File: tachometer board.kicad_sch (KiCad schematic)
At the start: 5 parts, among them J1 Conn_01x04

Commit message: Add README.md
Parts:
- R1, R2: Part Number (none) -> CRCW1210470RFKEA
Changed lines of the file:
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@@
     (pin "4")
     (instances
-      (project "protean board"
+      (project "tachometer board"
         (path "/e74b6ee1-b9f5-4a36-af13-778b210f46d3"
           (reference "U1") (unit 1)
@@
       (effects (font (size 1.27 1.27)) hide)
     )
-    (pin "1")
-    (pin "2")
-    (instances
-      (project "protean board"
+    (property "Part Number" "CRCW1210470RFKEA" (at 168.275 74.295 0)
+      (effects (font (size 1.27 1.27)) hide)
+    )
+    (pin "1")
+    (pin "2")
+    (instances
+      (project "tachometer board"
         (path "/e74b6ee1-b9f5-4a36-af13-778b210f46d3"
           (reference "R2") (unit 1)
@@
     (pin "1")
     (instances
-      (project "protean board"
+      (project "tachometer board"
         (path "/e74b6ee1-b9f5-4a36-af13-778b210f46d3"
           (reference "#PWR04") (unit 1)
@@
     (pin "1")
     (instances
-      (project "protean board"
+      (project "tachometer board"
         (path "/e74b6ee1-b9f5-4a36-af13-778b210f46d3"
           (reference "#PWR03") (unit 1)
@@
     (pin "4")
     (instances
-      (project "protean board"
+      (project "tachometer board"
         (path "/e74b6ee1-b9f5-4a36-af13-778b210f46d3"
           (reference "U2") (unit 1)
@@
     (pin "1")
     (instances
-      (project "protean board"
+      (project "tachometer board"
         (path "/e74b6ee1-b9f5-4a36-af13-778b210f46d3"
           (reference "#PWR02") (unit 1)
@@
     (pin "4")
     (instances
-      (project "protean board"
+      (project "tachometer board"
         (path "/e74b6ee1-b9f5-4a36-af13-778b210f46d3"
           (reference "J1") (unit 1)
@@
       (effects (font (size 1.27 1.27)) hide)
     )
-    (pin "1")
-    (pin "2")
-    (instances
-      (project "protean board"
+    (property "Part Number" "CRCW1210470RFKEA" (at 168.275 59.055 0)
+      (effects (font (size 1.27 1.27)) hide)
+    )
+    (pin "1")
+    (pin "2")
+    (instances
+      (project "tachometer board"
         (path "/e74b6ee1-b9f5-4a36-af13-778b210f46d3"
           (reference "R1") (unit 1)
@@
     (pin "1")
     (instances
-      (project "protean board"
+      (project "tachometer board"
         (path "/e74b6ee1-b9f5-4a36-af13-778b210f46d3"
           (reference "#PWR01") (unit 1)

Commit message: Add SAMD MCU and MOSFET
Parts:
- removed J1: Conn_01x04, JST_PH_S4B-PH-K_1x04_P2.00mm_Horizontal, symbol Connector_Generic:Conn_01x04
- added C1, C2, C3, C4, C5: C, Capacitor_SMD:C_0805_2012Metric, symbol Device:C
- added Q1: PSMN8R5-40MSDX, Package_TO_SOT_SMD:LFPAK33, symbol Transistor_FET:PSMN5R2-60YL
- added U3: ATSAMD21G18A-A, Package_QFP:TQFP-48_7x7mm_P0.5mm, symbol MCU_Microchip_SAMD:ATSAMD21G18A-A
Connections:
- net GND: now also C1.2, C2.2, C3.2, C4.2, C5.2
- net OUT1 renamed TACHA
- net OUT2 renamed TACHB
- new net: Q1.1 (S), Q1.2 (S), Q1.3 (S)
- new net: U3.18 (GND), U3.35 (GND), U3.42 (GND)
- new net +3V3: C1.1, C2.1, C3.1, C4.1, C5.1, U3.17 (VDDIO), U3.36 (VDDIO), U3.43 (VDDCORE), U3.44 (VDDIN), U3.6 (VDDANA)
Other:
- note added: "TODO: Double check symbol to footprint pin mapping for MOSFET is correct!"
- moved on the sheet: R1, R2, U1, U2

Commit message: Misc. changes to schematic and PCB
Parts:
- added D1, D2: LED, symbol Device:LED
- added J1: USB_B_Micro, Connector_USB:USB_Micro-B_Molex_47346-0001, symbol Connector:USB_B_Micro
- added J2: Conn_01x05_Pin, Marks Library:4mm_by_6mm_Solder_Pad_x5, symbol Connector:Conn_01x05_Pin
- added Q2: PSMN8R5-40MSX, Package_TO_SOT_SMD:LFPAK33, symbol Transistor_FET:PSMN5R2-60YL
- added R3, R4: R, symbol Device:R
- added R5: 100, symbol Device:R
- added SW1: SW_Push, symbol Switch:SW_Push
- added U4, U5: ZXGD3009DY, Package_TO_SOT_SMD:SOT-23-6, symbol Marks_Symbols:ZXGD3009DY
- added U6: AP2112K-3.3, Package_TO_SOT_SMD:SOT-23-5, symbol Regulator_Linear:AP2112K-3.3
- C1, C2, C3, C4: footprint Capacitor_SMD:C_0805_2012Metric -> Capacitor_SMD:C_0402_1005Metric
- C5: value C -> 1uF; footprint Capacitor_SMD:C_0805_2012Metric -> Capacitor_SMD:C_0402_1005Metric
- Q1: value PSMN8R5-40MSDX -> PSMN8R5-40MSX
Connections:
- net +3V3: now also U6.5 (VOUT); no longer C5.1, U3.43 (VDDCORE)
- net GND: now also Q1.1 (S), Q1.2 (S), Q1.3 (S), U3.18 (GND), U3.35 (GND), U3.42 (GND), U3.5 (GNDANA), D1.1 (K), D2.1 (K), J1.5 (GND), J1.6 (Shield), J2.2 (Pin_2), Q2.1 (S), Q2.2 (S), Q2.3 (S), SW1.2, U4.3 (GND), U5.3 (GND), U6.2 (GND)
- net TACHA: now also U3.26 (PA17)
- net TACHB: now also U3.25 (PA16)
- net GATEA: now reaches Q1.4 (G)
- net GATEA: now also U4.4 (SINK), U4.6 (SOURCE)
- net MOTORA-: now reaches Q1.5 (D)
- net MOTORA-: now also J2.3 (Pin_3)
- net USB_D-: now reaches U3.33 (PA24)
- net USB_D-: now also J1.2 (D-)
- net USB_D+: now reaches U3.34 (PA25)
- net USB_D+: now also J1.3 (D+)
- net RESET: now reaches U3.40 (~{RESET})
- net RESET: now also SW1.1
- new net: D1.2 (A), R3.2
- new net: C5.1, U3.43 (VDDCORE)
- new net: R5.1, U6.1 (VIN)
- new net: R5.2, U6.3 (EN)
- new net: D2.2 (A), R4.2
- new net +BATT: J2.1 (Pin_1), J2.4 (Pin_4), U4.1 (VCC), U5.1 (VCC)
- new net GATEB: Q2.4 (G), U5.4 (SINK), U5.6 (SOURCE)
- new net LED1: R3.1
- new net LED2: R4.1
- new net MOTORB-: J2.5 (Pin_5), Q2.5 (D)
- new net MOTOR_A_DRIVER_INPUT: U4.2 (IN1)
- new net MOTOR_B_DRIVER_INPUT: U5.2 (IN1)
- new net USB_VBUS: J1.1 (VBUS)
- no-connect marks 0 -> 1
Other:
- note added: "Notes to future self: - WAGO 2060-451/998-404 is a potential connector to use for the motor wires"
- note added: "TODO: Consider adding decoupling caps to Vin and Vout of LDO. Datasheet suggests one 1uF on each."
- moved on the sheet: C5, Q1

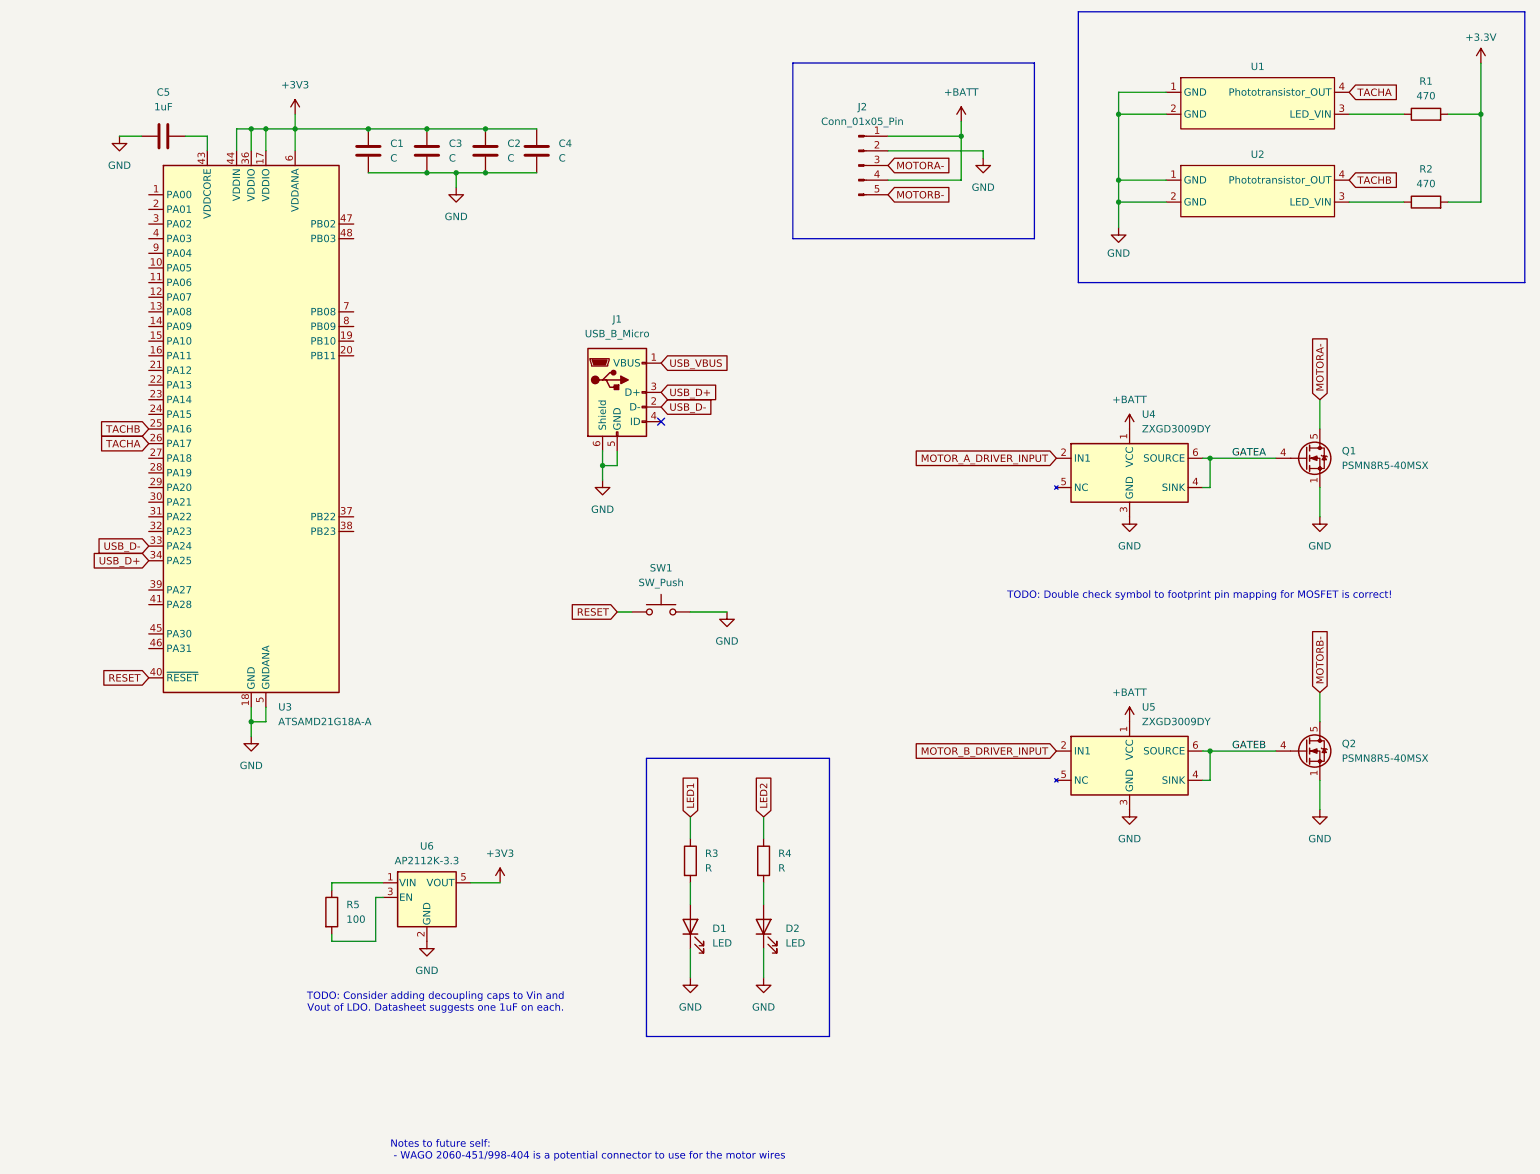
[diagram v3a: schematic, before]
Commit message: Add buck converter
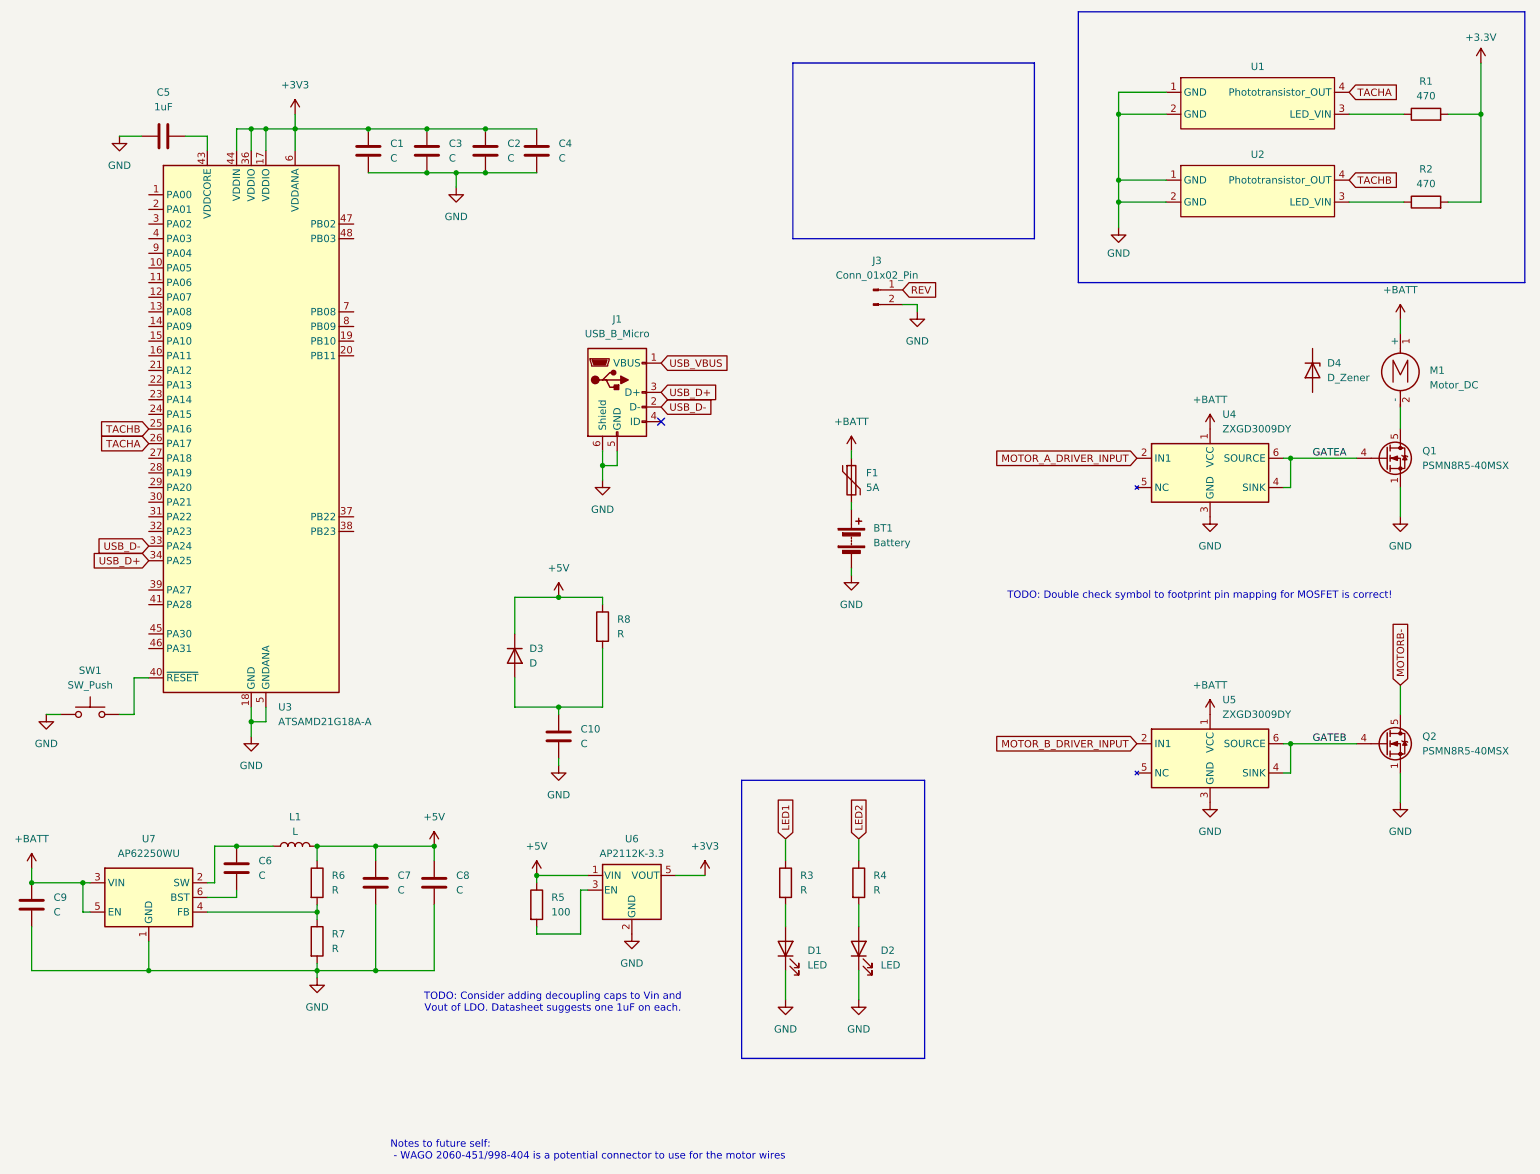
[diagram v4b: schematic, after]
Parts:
- removed J2: Conn_01x05_Pin, Marks Library:4mm_by_6mm_Solder_Pad_x5, symbol Connector:Conn_01x05_Pin
- added BT1: Battery, Connector_AMASS:AMASS_XT30PW-M_1x02_P2.50mm_Horizontal, symbol Device:Battery
- added C10, C6, C7, C8, C9: C, symbol Device:C
- added D3: D, symbol Device:D
- added D4: D_Zener, symbol Device:D_Zener
- added F1: 5A, Fuse:Fuse_2920_7451Metric, symbol Device:Polyfuse
- added J3: Conn_01x02_Pin, Connector_PinHeader_2.54mm:PinHeader_1x02_P2.54mm_Vertical, symbol Connector:Conn_01x02_Pin
- added L1: L, symbol Device:L
- added M1: Motor_DC, Marks Library:4mm_by_6mm_Solder_Pad_x2, symbol Motor:Motor_DC
- added R6, R7, R8: R, symbol Device:R
- added U7: AP62250WU, Package_TO_SOT_SMD:TSOT-23-6, symbol Regulator_Switching:AP62250WU
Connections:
- net +BATT: now also C9.1, F1.1, M1.1 (+), U7.3 (VIN), U7.5 (EN)
- net GND: now also SW1.1, BT1.2 (-), C10.2, C7.2, C8.2, C9.2, J3.2 (Pin_2), R7.2, U7.1 (GND); no longer SW1.2
- net +5V: now reaches R5.1, U6.1 (VIN)
- net +5V: now also C7.1, C8.1, D3.1 (K), L1.2, R6.1, R8.1
- net MOTORA-: no longer names the net of Q1.5 (D)
- net MOTORA-: now also M1.2 (-)
- net RESET: no longer names the net of U3.40 (~{RESET})
- net RESET: now also SW1.2; no longer SW1.1
- new net: C10.1, D3.2 (A), R8.2
- new net: R6.2, R7.1, U7.4 (FB)
- new net: C6.1, L1.1, U7.2 (SW)
- new net: C6.2, U7.6 (BST)
- new net: BT1.1 (+), F1.2
- new net REV: J3.1 (Pin_1)
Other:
- moved on the sheet: D1, D2, Q1, Q2, R3, R4, R5, SW1, U4, U5, U6

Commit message: Misc changes
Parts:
- C10: value C -> 470uF; footprint (none) -> Capacitor_SMD:CP_Elec_8x10
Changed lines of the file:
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@@
 	)
 	(symbol
+		(lib_name "IR_Reflectivity_Sensor_1")
 		(lib_id "Marks_Symbols:IR_Reflectivity_Sensor")
 		(at 233.68 31.75 0)
@@
 			)
 		)
-		(property "Value" "C"
+		(property "Value" "470uF"
 			(at 116.84 142.2399 0)
 			(effects
@@
 			)
 		)
-		(property "Footprint" ""
+		(property "Footprint" "Capacitor_SMD:CP_Elec_8x10"
 			(at 113.9952 144.78 0)
 			(effects
@@
 			(at 113.03 140.97 0)
 			(effects
+				(font
+					(size 1.27 1.27)
+				)
+				(hide yes)
+			)
+		)
+		(property "Part Number" ""
+			(at 113.03 140.97 0)
+			(effects
